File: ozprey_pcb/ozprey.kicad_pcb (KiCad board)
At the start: 2 copper layers, 256.1 x 99.3 mm, 97 parts, among them J1 Conn_01x02, J3 Conn_01x02_Male, SW1 CPG135001S30, SW10 CPG135001S30, SW11 CPG135001S30, SW12 CPG135001S30, SW13 CPG135001S30, SW14 CPG135001S30, SW15 CPG135001S30, SW16 CPG135001S30, SW17 CPG135001S30, SW18 CPG135001S30, SW19 CPG135001S30, SW2 CPG135001S30, SW20 CPG135001S30, SW21 CPG135001S30, SW22 CPG135001S30, SW23 CPG135001S30, SW24 CPG135001S30, SW25 CPG135001S30, SW26 CPG135001S30, SW27 CPG135001S30, SW28 CPG135001S30, SW29 CPG135001S30, SW3 CPG135001S30, SW30 CPG135001S30, SW31 CPG135001S30, SW32 CPG135001S30, SW33 CPG135001S30, SW34 CPG135001S30, SW35 CPG135001S30, SW36 CPG135001S30, SW37 CPG135001S30, SW38 CPG135001S30, SW39 CPG135001S30, SW4 CPG135001S30, SW40 CPG135001S30, SW41 CPG135001S30, SW42 CPG135001S30, SW43 SW_DPDT_x2, SW5 CPG135001S30, SW6 CPG135001S30, SW7 CPG135001S30, SW8 CPG135001S30, SW9 CPG135001S30, U1 nice_nano

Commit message: rework pcb, remove enclosure & plate folders
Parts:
- removed G***: cat, kapee-keeb-parts:cat
- removed G***: cat_m, kapee-keeb-parts:cat_m
- removed H1, H2, H3, H4, H5, H6: M2, MountingHole:MountingHole_2.2mm_M2_DIN965_Pad
- removed J1: Conn_01x02, Connector_JST:JST_ACH_BM02B-ACHSS-GAN-ETF_1x02-1MP_P1.20mm_Vertical
- removed J3: Conn_01x02_Male, acheron_Connectors.pretty-master:PinHeader_1x2_P2.54mm_Vertical
- removed REF**: kapee_logo, kapee-keeb-parts:kapee_logo
- removed SW43: SW_DPDT_x2, kapee-keeb-parts:MSK12C02
- added BATT1: Battery_Cell, Keyboard:Battery_pads, B.Cu at (149.2, 32.9)
- added SW_PWR1: SW_SPDT, Button_Switch_SMD:SW_SPDT_PCM12, B.Cu at (163.6, 30.9)
- added SW_RST1: SW_Push, Button_Switch_SMD:SW_SPST_TL3342, F.Cu at (134.2, 32.4)
- SW1: renamed from SW12; footprint kapee-keeb-parts:SW_choc_HS_1u -> Keyboard:Kailh_socket_Choc_optional; moved to F.Cu
- SW10: renamed from SW9; footprint kapee-keeb-parts:SW_choc_HS_1u -> Keyboard:Kailh_socket_Choc_optional; moved to F.Cu
- SW11: renamed from SW21; footprint kapee-keeb-parts:SW_choc_HS_1u -> Keyboard:Kailh_socket_Choc_optional; moved to F.Cu
- SW12: renamed from SW33; footprint kapee-keeb-parts:SW_choc_HS_1u -> Keyboard:Kailh_socket_Choc_optional; moved to F.Cu
- SW13: renamed from SW42; footprint kapee-keeb-parts:SW_choc_HS_1u -> Keyboard:Kailh_socket_Choc_optional; moved to F.Cu
- SW14: renamed from SW8; footprint kapee-keeb-parts:SW_choc_HS_1u -> Keyboard:Kailh_socket_Choc_optional; moved to F.Cu
- SW15: renamed from SW20; footprint kapee-keeb-parts:SW_choc_HS_1u -> Keyboard:Kailh_socket_Choc_optional; moved to F.Cu
- SW16: renamed from SW32; footprint kapee-keeb-parts:SW_choc_HS_1u -> Keyboard:Kailh_socket_Choc_optional; moved to F.Cu
- SW17: renamed from SW41; footprint kapee-keeb-parts:SW_choc_HS_1u -> Keyboard:Kailh_socket_Choc_optional; moved to F.Cu
- SW18: renamed from SW7; footprint kapee-keeb-parts:SW_choc_HS_1u -> Keyboard:Kailh_socket_Choc_optional; moved to F.Cu
- SW19: footprint kapee-keeb-parts:SW_choc_HS_1u -> Keyboard:Kailh_socket_Choc_optional; moved to F.Cu
- SW2: renamed from SW24; footprint kapee-keeb-parts:SW_choc_HS_1u -> Keyboard:Kailh_socket_Choc_optional; moved to F.Cu
- SW20: renamed from SW31; footprint kapee-keeb-parts:SW_choc_HS_1u -> Keyboard:Kailh_socket_Choc_optional; moved to F.Cu
- SW21: renamed from SW40; footprint kapee-keeb-parts:SW_choc_HS_1.5u -> Keyboard:Kailh_socket_Choc_optional; moved to F.Cu
- SW22: renamed from SW6; footprint kapee-keeb-parts:SW_choc_HS_1u -> Keyboard:Kailh_socket_Choc_optional; moved to F.Cu
- SW23: renamed from SW18; footprint kapee-keeb-parts:SW_choc_HS_1u -> Keyboard:Kailh_socket_Choc_optional; moved to F.Cu
- SW24: renamed from SW30; footprint kapee-keeb-parts:SW_choc_HS_1u -> Keyboard:Kailh_socket_Choc_optional; moved to F.Cu
- SW25: renamed from SW39; footprint kapee-keeb-parts:SW_choc_HS_1.5u -> Keyboard:Kailh_socket_Choc_optional; moved to F.Cu
- SW26: renamed from SW5; footprint kapee-keeb-parts:SW_choc_HS_1u -> Keyboard:Kailh_socket_Choc_optional; moved to F.Cu
- SW27: renamed from SW17; footprint kapee-keeb-parts:SW_choc_HS_1u -> Keyboard:Kailh_socket_Choc_optional; moved to F.Cu
- SW28: renamed from SW29; footprint kapee-keeb-parts:SW_choc_HS_1u -> Keyboard:Kailh_socket_Choc_optional; moved to F.Cu
- SW29: renamed from SW38; footprint kapee-keeb-parts:SW_choc_HS_1u -> Keyboard:Kailh_socket_Choc_optional; moved to F.Cu
- SW3: renamed from SW36; footprint kapee-keeb-parts:SW_choc_HS_1u -> Keyboard:Kailh_socket_Choc_optional; moved to F.Cu
- SW30: renamed from SW4; footprint kapee-keeb-parts:SW_choc_HS_1u -> Keyboard:Kailh_socket_Choc_optional; moved to F.Cu
- SW31: renamed from SW16; footprint kapee-keeb-parts:SW_choc_HS_1u -> Keyboard:Kailh_socket_Choc_optional; moved to F.Cu
- SW32: renamed from SW28; footprint kapee-keeb-parts:SW_choc_HS_1u -> Keyboard:Kailh_socket_Choc_optional; moved to F.Cu
- SW33: renamed from SW37; footprint kapee-keeb-parts:SW_choc_HS_1u -> Keyboard:Kailh_socket_Choc_optional; moved to F.Cu
- SW34: renamed from SW3; footprint kapee-keeb-parts:SW_choc_HS_1u -> Keyboard:Kailh_socket_Choc_optional; moved to F.Cu
- SW35: renamed from SW15; footprint kapee-keeb-parts:SW_choc_HS_1u -> Keyboard:Kailh_socket_Choc_optional; moved to F.Cu
- SW36: renamed from SW27; footprint kapee-keeb-parts:SW_choc_HS_1u -> Keyboard:Kailh_socket_Choc_optional; moved to F.Cu
- SW37: renamed from SW2; footprint kapee-keeb-parts:SW_choc_HS_1u -> Keyboard:Kailh_socket_Choc_optional; moved to F.Cu
- SW38: renamed from SW14; footprint kapee-keeb-parts:SW_choc_HS_1u -> Keyboard:Kailh_socket_Choc_optional; moved to F.Cu
- SW39: renamed from SW26; footprint kapee-keeb-parts:SW_choc_HS_1u -> Keyboard:Kailh_socket_Choc_optional; moved to F.Cu
- SW4: renamed from SW11; footprint kapee-keeb-parts:SW_choc_HS_1u -> Keyboard:Kailh_socket_Choc_optional; moved to F.Cu
- SW40: renamed from SW1; footprint kapee-keeb-parts:SW_choc_HS_1u -> Keyboard:Kailh_socket_Choc_optional; moved to F.Cu
- SW41: renamed from SW13; footprint kapee-keeb-parts:SW_choc_HS_1u -> Keyboard:Kailh_socket_Choc_optional; moved to F.Cu
- SW42: renamed from SW25; footprint kapee-keeb-parts:SW_choc_HS_1u -> Keyboard:Kailh_socket_Choc_optional; moved to F.Cu
- SW5: renamed from SW23; footprint kapee-keeb-parts:SW_choc_HS_1u -> Keyboard:Kailh_socket_Choc_optional; moved to F.Cu
- SW6: renamed from SW35; footprint kapee-keeb-parts:SW_choc_HS_1u -> Keyboard:Kailh_socket_Choc_optional; moved to F.Cu
- SW7: renamed from SW10; footprint kapee-keeb-parts:SW_choc_HS_1u -> Keyboard:Kailh_socket_Choc_optional; moved to F.Cu
- SW8: renamed from SW22; footprint kapee-keeb-parts:SW_choc_HS_1u -> Keyboard:Kailh_socket_Choc_optional; moved to F.Cu
- SW9: renamed from SW34; footprint kapee-keeb-parts:SW_choc_HS_1u -> Keyboard:Kailh_socket_Choc_optional; moved to F.Cu
- U1: footprint kapee-keeb-parts:NiceNano -> ProMicro:nice_nano
- moved SW42 238.2 mm to (268.2, 69.2), turned to 18 degrees
- moved SW3 230.8 mm to (30.0, 69.2), turned to -18 degrees
- moved SW41 227.7 mm to (263.0, 53.0), turned to 18 degrees
- moved SW2 220.3 mm to (35.3, 53.0), turned to -18 degrees
- moved SW40 217.2 mm to (257.7, 36.9), turned to 18 degrees
- moved SW1 209.8 mm to (40.5, 36.9), turned to -18 degrees
- moved SW39 201.3 mm to (249.8, 70.8), turned to 18 degrees
- moved SW6 194.0 mm to (48.5, 70.8), turned to -18 degrees
- moved SW38 190.8 mm to (244.5, 54.6), turned to 18 degrees
- moved SW5 183.5 mm to (53.7, 54.6), turned to -18 degrees
- moved SW37 180.3 mm to (239.3, 38.4), turned to 18 degrees
- moved SW4 173.0 mm to (59.0, 38.4), turned to -18 degrees
- moved SW36 164.5 mm to (231.4, 72.3), turned to 18 degrees
- moved SW9 157.1 mm to (66.9, 72.3), turned to -18 degrees
- moved SW35 154.0 mm to (226.1, 56.2), turned to 18 degrees
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- renumbered D4 to D10, D16 to D11, D28 to D12, D37 to D13, D5 to D14, D17 to D15, D29 to D16, D38 to D17, D6 to D18, D18 to D19, D13 to D2, D30 to D20, D39 to D21, D7 to D22, D19 to D23, D31 to D24, D40 to D25, D8 to D26, D20 to D27, D32 to D28, D41 to D29, D25 to D3, D9 to D30, D21 to D31, D33 to D32, D42 to D33, D10 to D34, D22 to D35, D34 to D36, D11 to D37, D23 to D38, D35 to D39, D2 to D4, D12 to D40, D24 to D41, D36 to D42, D14 to D5, D26 to D6, D3 to D7, D15 to D8, D27 to D9
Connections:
- D10 pad 2: Net-(D4-A) -> Net-(D10-A)
- D11 pad 2: Net-(D16-A) -> Net-(D11-A)
- D12 pad 2: Net-(D28-A) -> Net-(D12-A)
- D13 pad 2: Net-(D37-A) -> Net-(D13-A)
- D14 pad 2: Net-(D5-A) -> Net-(D14-A)
- D15 pad 2: Net-(D17-A) -> Net-(D15-A)
- D16 pad 2: Net-(D29-A) -> Net-(D16-A)
- D17 pad 2: Net-(D38-A) -> Net-(D17-A)
- D18 pad 2: Net-(D6-A) -> Net-(D18-A)
- D19 pad 2: Net-(D18-A) -> Net-(D19-A)
- D2 pad 2: Net-(D13-A) -> Net-(D2-A)
- D20 pad 2: Net-(D30-A) -> Net-(D20-A)
- D21 pad 2: Net-(D39-A) -> Net-(D21-A)
- D22 pad 2: Net-(D7-A) -> Net-(D22-A)
- D23 pad 2: Net-(D19-A) -> Net-(D23-A)
- D24 pad 2: Net-(D31-A) -> Net-(D24-A)
- D25 pad 2: Net-(D40-A) -> Net-(D25-A)
- D26 pad 2: Net-(D8-A) -> Net-(D26-A)
- D27 pad 2: Net-(D20-A) -> Net-(D27-A)
- D28 pad 2: Net-(D32-A) -> Net-(D28-A)
- D29 pad 2: Net-(D41-A) -> Net-(D29-A)
- D3 pad 2: Net-(D25-A) -> Net-(D3-A)
- D30 pad 2: Net-(D9-A) -> Net-(D30-A)
- D31 pad 2: Net-(D21-A) -> Net-(D31-A)
- D32 pad 2: Net-(D33-A) -> Net-(D32-A)
- D33 pad 2: Net-(D42-A) -> Net-(D33-A)
- D34 pad 2: Net-(D10-A) -> Net-(D34-A)
- D35 pad 2: Net-(D22-A) -> Net-(D35-A)
- D36 pad 2: Net-(D34-A) -> Net-(D36-A)
- D37 pad 2: Net-(D11-A) -> Net-(D37-A)
- D38 pad 2: Net-(D23-A) -> Net-(D38-A)
- D39 pad 2: Net-(D35-A) -> Net-(D39-A)
- D4 pad 2: Net-(D2-A) -> Net-(D4-A)
- D40 pad 2: Net-(D12-A) -> Net-(D40-A)
- D41 pad 2: Net-(D24-A) -> Net-(D41-A)
- D42 pad 2: Net-(D36-A) -> Net-(D42-A)
- D5 pad 2: Net-(D14-A) -> Net-(D5-A)
- D6 pad 2: Net-(D26-A) -> Net-(D6-A)
- D7 pad 2: Net-(D3-A) -> Net-(D7-A)
- D8 pad 2: Net-(D15-A) -> Net-(D8-A)
- D9 pad 2: Net-(D27-A) -> Net-(D9-A)
- SW1 pad 1: COL11 -> COL0
- SW1 pad 2: Net-(D12-A) -> Net-(D1-A)
- SW10 pad 1: COL8 -> COL3
- SW10 pad 2: Net-(D9-A) -> Net-(D10-A)
- SW11 pad 1: COL8 -> COL3
- SW11 pad 2: Net-(D21-A) -> Net-(D11-A)
- SW12 pad 1: COL8 -> COL3
- SW12 pad 2: Net-(D33-A) -> Net-(D12-A)
- SW13 pad 1: COL8 -> COL3
- SW13 pad 2: Net-(D42-A) -> Net-(D13-A)
- SW14 pad 1: COL7 -> COL4
- SW14 pad 2: Net-(D8-A) -> Net-(D14-A)
- SW15 pad 1: COL7 -> COL4
- SW15 pad 2: Net-(D20-A) -> Net-(D15-A)
- SW16 pad 1: COL7 -> COL4
- SW16 pad 2: Net-(D32-A) -> Net-(D16-A)
- SW17 pad 1: COL7 -> COL4
- SW17 pad 2: Net-(D41-A) -> Net-(D17-A)
- SW18 pad 1: COL6 -> COL5
- SW18 pad 2: Net-(D7-A) -> Net-(D18-A)
- SW19 pad 1: COL6 -> COL5
- SW2 pad 1: COL11 -> COL0
- SW2 pad 2: Net-(D24-A) -> Net-(D2-A)
- SW20 pad 1: COL6 -> COL5
- SW20 pad 2: Net-(D31-A) -> Net-(D20-A)
- SW21 pad 1: COL6 -> COL5
- SW21 pad 2: Net-(D40-A) -> Net-(D21-A)
- SW22 pad 1: COL5 -> COL6
- SW22 pad 2: Net-(D6-A) -> Net-(D22-A)
- SW23 pad 1: COL5 -> COL6
- SW23 pad 2: Net-(D18-A) -> Net-(D23-A)
- SW24 pad 1: COL5 -> COL6
- SW24 pad 2: Net-(D30-A) -> Net-(D24-A)
- SW25 pad 1: COL5 -> COL6
- SW25 pad 2: Net-(D39-A) -> Net-(D25-A)
- SW26 pad 1: COL4 -> COL7
- SW26 pad 2: Net-(D5-A) -> Net-(D26-A)
- SW27 pad 1: COL4 -> COL7
- SW27 pad 2: Net-(D17-A) -> Net-(D27-A)
- SW28 pad 1: COL4 -> COL7
- SW28 pad 2: Net-(D29-A) -> Net-(D28-A)
- SW29 pad 1: COL4 -> COL7
- SW29 pad 2: Net-(D38-A) -> Net-(D29-A)
- SW3 pad 1: COL11 -> COL0
- SW3 pad 2: Net-(D36-A) -> Net-(D3-A)
- SW30 pad 1: COL3 -> COL8
- SW30 pad 2: Net-(D4-A) -> Net-(D30-A)
- SW31 pad 1: COL3 -> COL8
- SW31 pad 2: Net-(D16-A) -> Net-(D31-A)
- SW32 pad 1: COL3 -> COL8
- SW32 pad 2: Net-(D28-A) -> Net-(D32-A)
- SW33 pad 1: COL3 -> COL8
- SW33 pad 2: Net-(D37-A) -> Net-(D33-A)
- SW34 pad 1: COL2 -> COL9
- SW34 pad 2: Net-(D3-A) -> Net-(D34-A)
- SW35 pad 1: COL2 -> COL9
- SW35 pad 2: Net-(D15-A) -> Net-(D35-A)
- SW36 pad 1: COL2 -> COL9
- SW36 pad 2: Net-(D27-A) -> Net-(D36-A)
- SW37 pad 1: COL1 -> COL10
- SW37 pad 2: Net-(D2-A) -> Net-(D37-A)
- SW38 pad 1: COL1 -> COL10
- SW38 pad 2: Net-(D14-A) -> Net-(D38-A)
- SW39 pad 1: COL1 -> COL10
- SW39 pad 2: Net-(D26-A) -> Net-(D39-A)
- SW4 pad 1: COL10 -> COL1
- SW4 pad 2: Net-(D11-A) -> Net-(D4-A)
- SW40 pad 1: COL0 -> COL11
- SW40 pad 2: Net-(D1-A) -> Net-(D40-A)
- SW41 pad 1: COL0 -> COL11
- SW41 pad 2: Net-(D13-A) -> Net-(D41-A)
- SW42 pad 1: COL0 -> COL11
- SW42 pad 2: Net-(D25-A) -> Net-(D42-A)
- SW5 pad 1: COL10 -> COL1
- SW5 pad 2: Net-(D23-A) -> Net-(D5-A)
- SW6 pad 1: COL10 -> COL1
- SW6 pad 2: Net-(D35-A) -> Net-(D6-A)
- SW7 pad 1: COL9 -> COL2
- SW7 pad 2: Net-(D10-A) -> Net-(D7-A)
- SW8 pad 1: COL9 -> COL2
- SW8 pad 2: Net-(D22-A) -> Net-(D8-A)
- SW9 pad 1: COL9 -> COL2
- SW9 pad 2: Net-(D34-A) -> Net-(D9-A)
- U1 pad 22: unconnected-(U1-RST-Pad22) -> RST
- U1 pad 24: unconnected-(U1-BATIN/P0.04-Pad24) -> RAW
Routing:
- net GND: track 108.3 -> 40.5 mm, vias 1 -> 0
- net Bat+: track 53.5 -> 0.00 mm, vias 2 -> 0
- net ROW2: track 287.4 -> 336.2 mm, vias 1 -> 0
- net COL3: track 112.4 -> 160.5 mm, vias 4 -> 3
- net ROW1: track 258.7 -> 294.1 mm, vias 1 -> 0
- net COL5: track 77.6 -> 109.3 mm, vias 4 -> 1
- net COL1: track 132.6 -> 162.9 mm
- net COL2: track 114.2 -> 144.0 mm, vias 3 -> 2
- net RST: track 0.00 -> 29.4 mm
- net COL9: track 98.6 -> 127.1 mm
- net COL4: track 100.9 -> 126.4 mm, vias 4 -> 1
- net ROW3: track 205.3 -> 230.0 mm, vias 1 -> 0
- net COL11: track 138.9 -> 160.9 mm, vias 3 -> 0
- net COL7: track 87.9 -> 109.7 mm, vias 4 -> 3
- net COL6: track 65.3 -> 87.0 mm, vias 4 -> 2
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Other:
- board size 256.1 x 99.3 mm -> 263.5 x 99.3 mm
- board text added: "by itsdmd"
- board text added: "ozprey"
- board text removed: "osprey"

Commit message: update doc
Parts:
- added H_M2_1: MountingHole, MountingHole:MountingHole_2.2mm_M2, F.Cu at (66.4, 53.7)
- added H_M2_2: MountingHole, MountingHole:MountingHole_2.2mm_M2, F.Cu at (56.9, 108.2)
- added H_M2_3: MountingHole, MountingHole:MountingHole_2.2mm_M2, F.Cu at (120.4, 62.7)
- added H_M2_4: MountingHole, MountingHole:MountingHole_2.2mm_M2, F.Cu at (176.4, 62.7)
- added H_M2_5: MountingHole, MountingHole:MountingHole_2.2mm_M2, F.Cu at (230.4, 53.7)
- added H_M2_6: MountingHole, MountingHole:MountingHole_2.2mm_M2, F.Cu at (244.4, 108.2)
- added H_M2_7: MountingHole, MountingHole:MountingHole_2.2mm_M2, F.Cu at (148.9, 137.7)
- SW_PWR1: moved to F.Cu
- moved SW_PWR1 39.2 mm to (132.7, 55.1), turned to 180 degrees
- moved SW_RST1 38.4 mm to (164.2, 56.4), turned to 0 degrees
- moved D1 24.2 mm to (46.6, 68.2)
- moved D10 24.2 mm to (101.8, 72.9)
- moved D12 24.2 mm to (91.3, 105.2)
- moved D13 24.2 mm to (86.1, 121.4)
- moved D15 24.2 mm to (112.4, 98.6)
- moved D18 24.2 mm to (133.5, 92.0)
- moved D20 24.2 mm to (123.0, 124.3)
- moved D21 24.2 mm to (122.0, 141.9)
- moved D23 24.2 mm to (168.6, 108.3)
- moved D24 24.2 mm to (173.8, 124.5)
- moved D26 24.2 mm to (179.1, 82.6)
- moved D27 24.2 mm to (184.4, 98.8)
- moved D28 24.2 mm to (189.6, 114.9)
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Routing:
- net RST: track 29.4 -> 12.9 mm
- net COL8: track 118.5 -> 122.6 mm
- net GND: track 40.5 -> 43.6 mm
- net Net-(BATT1--): track 17.0 -> 18.7 mm, vias 2 -> 1
- net COL11: track 160.9 -> 160.3 mm
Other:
- outline, holes or cut-outs redrawn
- board text added: "ON"
- board text added: "Reset"

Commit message: add gerber
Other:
- board text added: "OFF"
- board text added: "PCM12"
- board text added: "RST"
- board text added: "TL3342"
- board text removed: "ON"
- board text removed: "Reset"
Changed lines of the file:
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@@
 			(at 0 -8.255 18)
 			(layer "F.SilkS")
+			(hide yes)
 			(effects
 				(font
@@
 			(at 0 -8.255 18)
 			(layer "F.SilkS")
+			(hide yes)
 			(effects
 				(font
@@
 			(at 0 -8.255 18)
 			(layer "F.SilkS")
+			(hide yes)
 			(effects
 				(font
@@
 			(at 0 -8.255 18)
 			(layer "F.SilkS")
+			(hide yes)
 			(effects
 				(font
@@
 			(at 0 -8.255 18)
 			(layer "F.SilkS")
+			(hide yes)
 			(effects
 				(font
@@
 			(at 0 -8.255 18)
 			(layer "F.SilkS")
+			(hide yes)
 			(effects
 				(font
@@
 			(at 0 -8.255 162)
 			(layer "F.SilkS")
+			(hide yes)
 			(effects
 				(font
@@
 			(at 0 -8.255 162)
 			(layer "F.SilkS")
+			(hide yes)
 			(effects
 				(font
@@
 			(at 0 -8.255 162)
 			(layer "F.SilkS")
+			(hide yes)
 			(effects
 				(font
@@
 			(at 0 -8.255 162)
 			(layer "F.SilkS")
+			(hide yes)
 			(effects
 				(font
@@
 			(at 0 -8.255 162)
 			(layer "F.SilkS")
+			(hide yes)
 			(effects
 				(font
@@
 			(at 0 -8.255 162)
 			(layer "F.SilkS")
+			(hide yes)
 			(effects
 				(font
@@
 			(at 0 -8.255 18)
 			(layer "F.SilkS")
+			(hide yes)
 			(effects
 				(font
@@
 			(at 0 -8.255 18)
 			(layer "F.SilkS")
+			(hide yes)
 			(effects
 				(font
@@
 			(at 0 -8.255 18)
 			(layer "F.SilkS")
+			(hide yes)
 			(effects
 				(font
@@
 			(at 0 -8.255 18)
 			(layer "F.SilkS")
+			(hide yes)
 			(effects
 				(font
@@
 			(at 0 -8.255 18)
 			(layer "F.SilkS")
+			(hide yes)
 			(effects
 				(font
@@
 			(at 0 -8.255 18)
 			(layer "F.SilkS")
+			(hide yes)
 			(effects
 				(font
@@
 			(at 0 -8.255 162)
 			(layer "F.SilkS")
+			(hide yes)
 			(effects
 				(font
@@
 			(at 0 -8.255 162)
 			(layer "F.SilkS")
+			(hide yes)
 			(effects
 				(font
@@
 			(at 0 -8.255 162)
 			(layer "F.SilkS")
+			(hide yes)
 			(effects
 				(font
@@
 			(at 0 -8.255 162)
 			(layer "F.SilkS")
+			(hide yes)
 			(effects
 				(font
@@
 			(at 0 -8.255 162)
 			(layer "F.SilkS")
+			(hide yes)
 			(effects
 				(font
@@
 			(at 0 -8.255 162)
 			(layer "F.SilkS")
+			(hide yes)
 			(effects
 				(font
@@
 			(at 0 -8.255 18)
 			(layer "F.SilkS")
+			(hide yes)
 			(effects
 				(font
@@
 			(at 0 -8.255 18)
 			(layer "F.SilkS")
+			(hide yes)
 			(effects
 				(font
@@
 			(at 0 -8.255 18)
 			(layer "F.SilkS")
+			(hide yes)
 			(effects
 				(font
@@
 			(at 0 -8.255 18)
 			(layer "F.SilkS")
+			(hide yes)
 			(effects
 				(font
@@
 			(at 0 -8.255 18)
 			(layer "F.SilkS")
+			(hide yes)
 			(effects
 				(font
@@
 			(at 0 -8.255 18)
 			(layer "F.SilkS")
+			(hide yes)
 			(effects
 				(font
@@
 			(at 0 -8.255 162)
 			(layer "F.SilkS")
+			(hide yes)
 			(effects
 				(font
@@
 			(at 0 -8.255 162)
 			(layer "F.SilkS")
+			(hide yes)
 			(effects
 				(font
@@
 			(at 0 -8.255 162)
 			(layer "F.SilkS")
+			(hide yes)
 			(effects
 				(font
@@
 			(at 0 -8.255 162)
 			(layer "F.SilkS")
+			(hide yes)
 			(effects
 				(font
@@
 			(at 0 -8.255 162)
 			(layer "F.SilkS")
+			(hide yes)
 			(effects
 				(font
@@
 			(at 0 -8.255 162)
 			(layer "F.SilkS")
+			(hide yes)
 			(effects
 				(font
@@
 			(at 0 -8.255 18)
 			(layer "F.SilkS")
+			(hide yes)
 			(effects
 				(font
@@
 			(at 0 -8.255 18)
 			(layer "F.SilkS")
+			(hide yes)
 			(effects
 				(font
@@
 			(at 0 -8.255 162)
 			(layer "F.SilkS")
+			(hide yes)
 			(effects
 				(font
@@
 			(at 0 -8.255 162)
 			(layer "F.SilkS")
+			(hide yes)
 			(effects
 				(font
@@
 			(at 0 -8.255 18)
 			(layer "F.SilkS")
+			(hide yes)
 			(effects
 				(font
@@
 			(at 0 -8.255 162)
 			(layer "F.SilkS")
+			(hide yes)
 			(effects
 				(font
@@
 		(layer "Edge.Cuts")
 	)
-	(gr_text "Reset"
-		(at 168.715469 56.877832 -0)
+	(gr_text "+"
+		(at 148.215469 103.877832 0)
 		(layer "B.SilkS")
 		(effects
 			(font
-				(size 1 1)
+				(size 0.8 0.8)
 				(thickness 0.15)
 			)
+		)
+	)
+	(gr_text "PCM12"
+		(at 130.715469 54.377832 0)
+		(layer "F.SilkS")
+		(effects
+			(font
+				(size 0.8 0.8)
+				(thickness 0.15)
+				(bold yes)
+			)
 			(justify left bottom)
 		)
 	)
-	(gr_text "+"
-		(at 148.215469 103.877832 0)
-		(layer "B.SilkS")
+	(gr_text "TL3342"
+		(at 162.081147 56.922605 0)
+		(layer "F.SilkS")
 		(effects
 			(font
 				(size 0.8 0.8)
 				(thickness 0.15)
+				(bold yes)
 			)
+			(justify left bottom)
 		)
 	)
@@
 		)
 	)
+	(gr_text "OFF"
+		(at 136.715469 55.169672 0)
+		(layer "F.SilkS")
+		(effects
+			(font
+				(size 0.8 0.8)
+				(thickness 0.15)
+				(bold yes)
+			)
+			(justify left bottom)
+		)
+	)
 	(gr_text "ozprey"
 		(at 149.001043 146.599704 0)
@@
 		)
 	)
-	(gr_text "ON"
-		(at 125.715469 55.377832 0)
+	(gr_text "RST"
+		(at 158.215469 56.877832 0)
 		(layer "F.SilkS")
 		(effects
 			(font
-				(size 1 1)
+				(size 0.8 0.8)
 				(thickness 0.15)
+				(bold yes)
 			)
 			(justify left bottom)

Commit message: update m2 holes pos
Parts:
- moved H_M2_1 19.9 mm to (86.2, 55.4)
- moved H_M2_5 19.7 mm to (210.7, 55.4)
- moved H_M2_3 12.3 mm to (132.7, 63.4)
- moved H_M2_4 12.2 mm to (164.2, 63.4)
- moved H_M2_6 4.49 mm to (240.2, 109.9)
- moved H_M2_2 1.65 mm to (56.9, 109.9)
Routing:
- net COL9: track 127.0 -> 126.3 mm

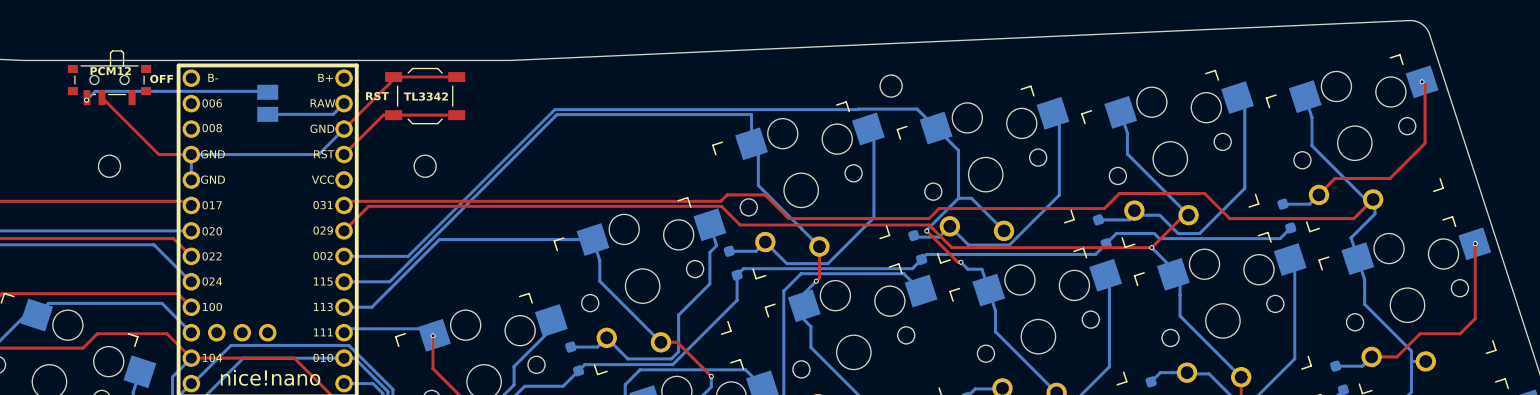
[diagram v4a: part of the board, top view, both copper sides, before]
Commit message: replace power & reset switches
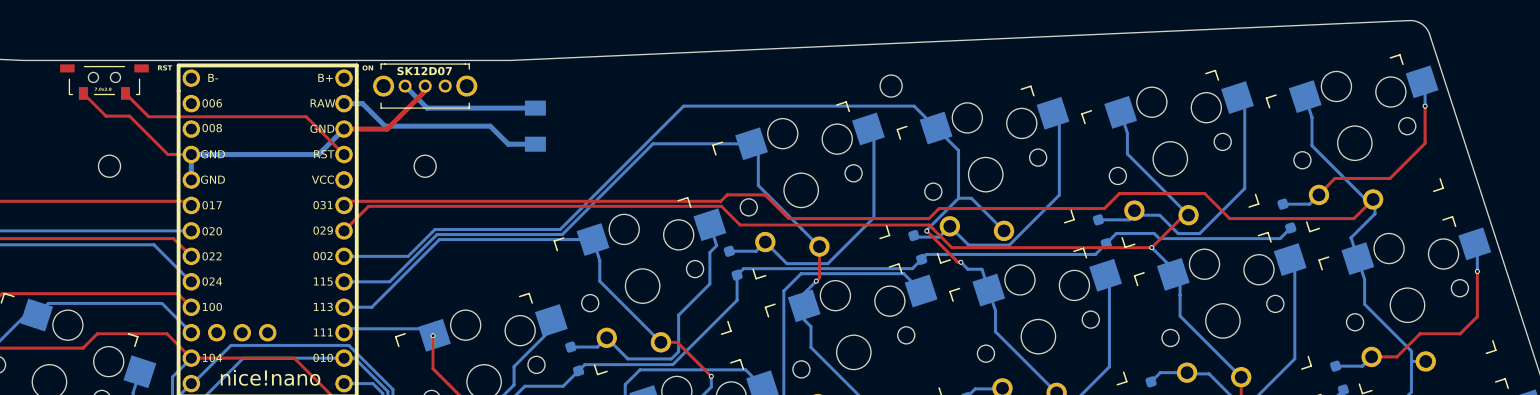
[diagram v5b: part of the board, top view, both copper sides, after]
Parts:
- removed SW_PWR1: SW_SPDT, Button_Switch_SMD:SW_SPDT_PCM12
- added SW43: SK12D07VG4, Switch:SK12D07VG4, F.Cu at (164.2, 55.4)
- SW_RST1: footprint Button_Switch_SMD:SW_SPST_TL3342 -> Switch:KG1
- moved SW_RST1 32.1 mm to (132.2, 54.4), turned to 180 degrees
- moved BATT1 26.8 mm to (175.2, 59.4)
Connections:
- SW_RST1 pad 1: GND -> RST
- SW_RST1 pad 2: RST -> GND
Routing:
- net RAW: track 8.06 -> 20.8 mm
- net RST: track 12.9 -> 24.3 mm
- net Net-(BATT1--): track 18.7 -> 13.9 mm, vias 1 -> 0
- net COL8: track 122.6 -> 118.5 mm
- net GND: track 43.6 -> 42.3 mm
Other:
- board text added: "7.0x2.8"
- board text added: "ON"
- board text added: "SK12D07"
- board text removed: "OFF"
- board text removed: "PCM12"
- board text removed: "TL3342"
